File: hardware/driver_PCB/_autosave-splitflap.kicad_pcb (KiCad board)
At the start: 2 copper layers, 111.8 x 95.2 mm, 19 parts, among them IC1 CD4049UBE, IC2 CD4049UBE, J1 Conn_02x06_Odd_Even, J2 Conn_02x06_Odd_Even, J3 Conn_01x16_Female, U1 74HC595, U2 74HC595, U3 SN754410NE, U4 SN754410NE, U5 SN754410NE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

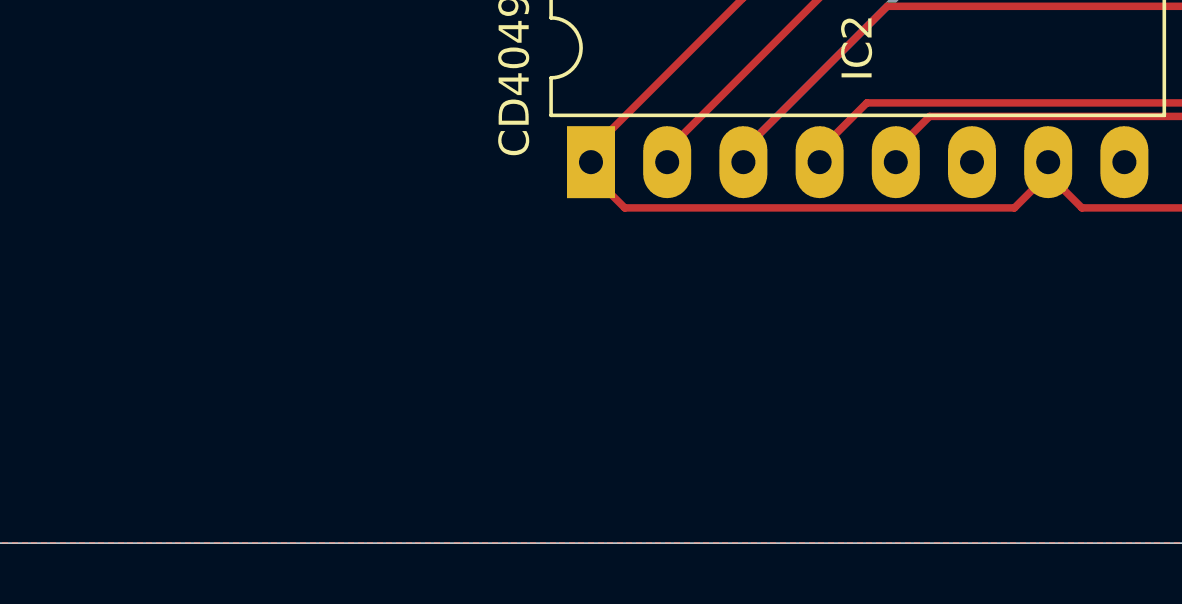
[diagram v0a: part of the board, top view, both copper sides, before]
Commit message: added functionality to read from serial
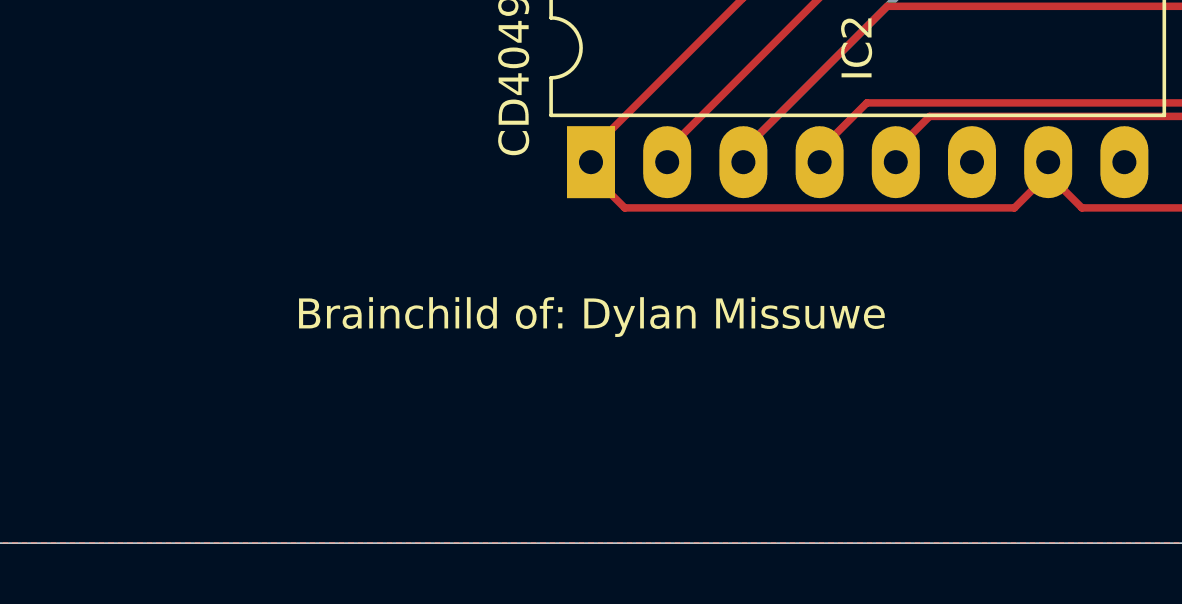
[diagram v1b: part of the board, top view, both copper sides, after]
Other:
- board text added: "Brainchild of: Dylan Missuwe"
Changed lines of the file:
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@@
   (general
     (thickness 1.6)
-    (drawings 57)
+    (drawings 58)
     (tracks 809)
     (zones 0)
@@
     )
   )
+  (gr_text "Brainchild of: Dylan Missuwe" (at 175.26 113.03) (layer F.SilkS)
+    (effects (font (size 1 1) (thickness 0.15)))
+  )
   (gr_text 74HC595 (at 172.72 83.82 90) (layer F.SilkS)

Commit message: some code cleanup
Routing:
- net (no net): vias 17 -> 0
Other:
- board text added: "brainchild of Dylan Missuwe"
- board text removed: "Brainchild of: Dylan Missuwe"
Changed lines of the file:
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@@
     (thickness 1.6)
     (drawings 58)
-    (tracks 809)
+    (tracks 792)
     (zones 0)
     (modules 19)
@@
     )
   )
-  (gr_text "Brainchild of: Dylan Missuwe" (at 175.26 113.03) (layer F.SilkS)
+  (gr_text "brainchild of Dylan Missuwe" (at 196.85 114.3) (layer F.SilkS)
     (effects (font (size 1 1) (thickness 0.15)))
   )
@@
   (gr_line (start 259.08 120.65) (end 147.32 120.65) (layer Edge.Cuts) (width 0.05))
   (gr_line (start 259.08 39.37) (end 259.08 120.65) (layer Edge.Cuts) (width 0.05))
-  (via (at 360.68 81.28) (size 0.8) (drill 0.4) (layers F.Cu B.Cu) (net 0))
-  (via (at 360.68 81.28) (size 0.8) (drill 0.4) (layers F.Cu B.Cu) (net 0))
-  (via (at 360.68 81.28) (size 0.8) (drill 0.4) (layers F.Cu B.Cu) (net 0))
-  (via (at 360.68 81.28) (size 0.8) (drill 0.4) (layers F.Cu B.Cu) (net 0))
-  (via (at 360.68 81.28) (size 0.8) (drill 0.4) (layers F.Cu B.Cu) (net 0))
-  (via (at 360.68 81.28) (size 0.8) (drill 0.4) (layers F.Cu B.Cu) (net 0))
-  (via (at 360.68 81.28) (size 0.8) (drill 0.4) (layers F.Cu B.Cu) (net 0))
-  (via (at 360.68 81.28) (size 0.8) (drill 0.4) (layers F.Cu B.Cu) (net 0))
-  (via (at 360.68 81.28) (size 0.8) (drill 0.4) (layers F.Cu B.Cu) (net 0))
-  (via (at 360.68 81.28) (size 0.8) (drill 0.4) (layers F.Cu B.Cu) (net 0))
-  (via (at 360.68 81.28) (size 0.8) (drill 0.4) (layers F.Cu B.Cu) (net 0))
-  (via (at 360.68 81.28) (size 0.8) (drill 0.4) (layers F.Cu B.Cu) (net 0))
-  (via (at 360.68 81.28) (size 0.8) (drill 0.4) (layers F.Cu B.Cu) (net 0))
-  (via (at 360.68 81.28) (size 0.8) (drill 0.4) (layers F.Cu B.Cu) (net 0))
-  (via (at 360.68 81.28) (size 0.8) (drill 0.4) (layers F.Cu B.Cu) (net 0))
-  (via (at 360.68 81.28) (size 0.8) (drill 0.4) (layers F.Cu B.Cu) (net 0))
-  (via (at 360.68 81.28) (size 0.8) (drill 0.4) (layers F.Cu B.Cu) (net 0))
   (segment (start 226.06 98.32) (end 226.06 96.52) (width 1) (layer F.Cu) (net 1))
   (segment (start 227.560001 99.820001) (end 226.06 98.32) (width 1) (layer F.Cu) (net 1))
